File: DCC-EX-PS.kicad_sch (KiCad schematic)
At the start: 8 parts, among them J1 54-00129, J2 OSTVN03A150, U1 TSR 0.5-2450, U2 TSR 2-24120

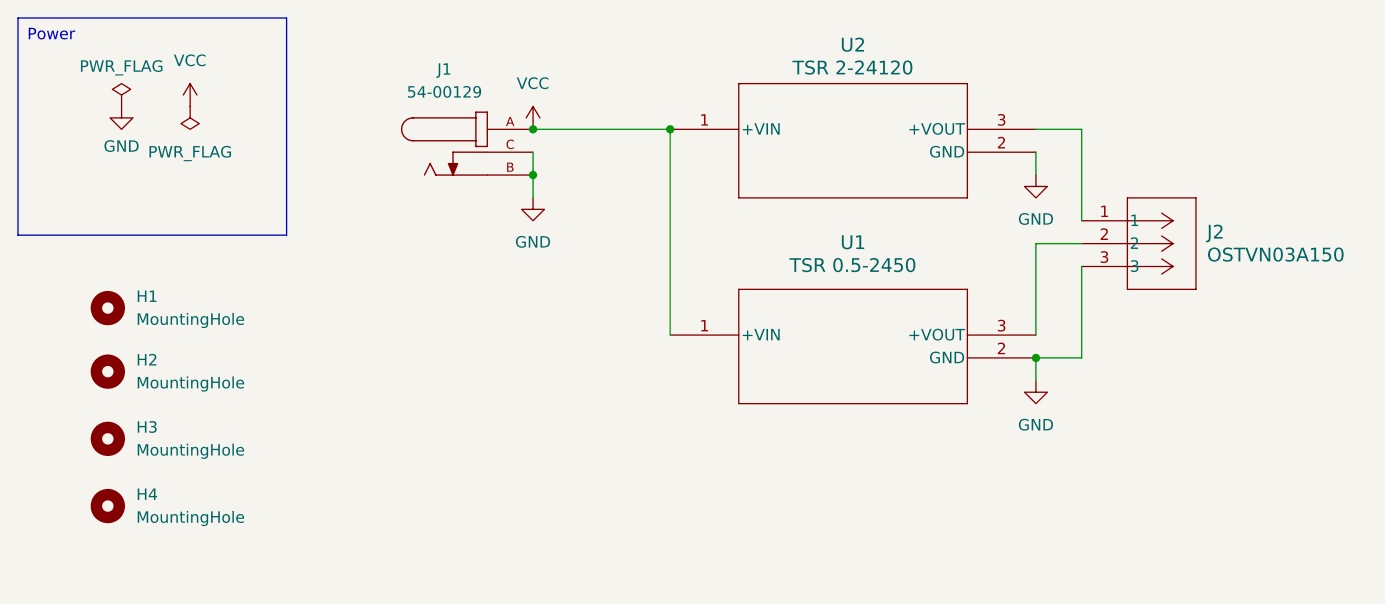
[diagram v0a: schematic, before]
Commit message: Added more graphics and 24v out terminal
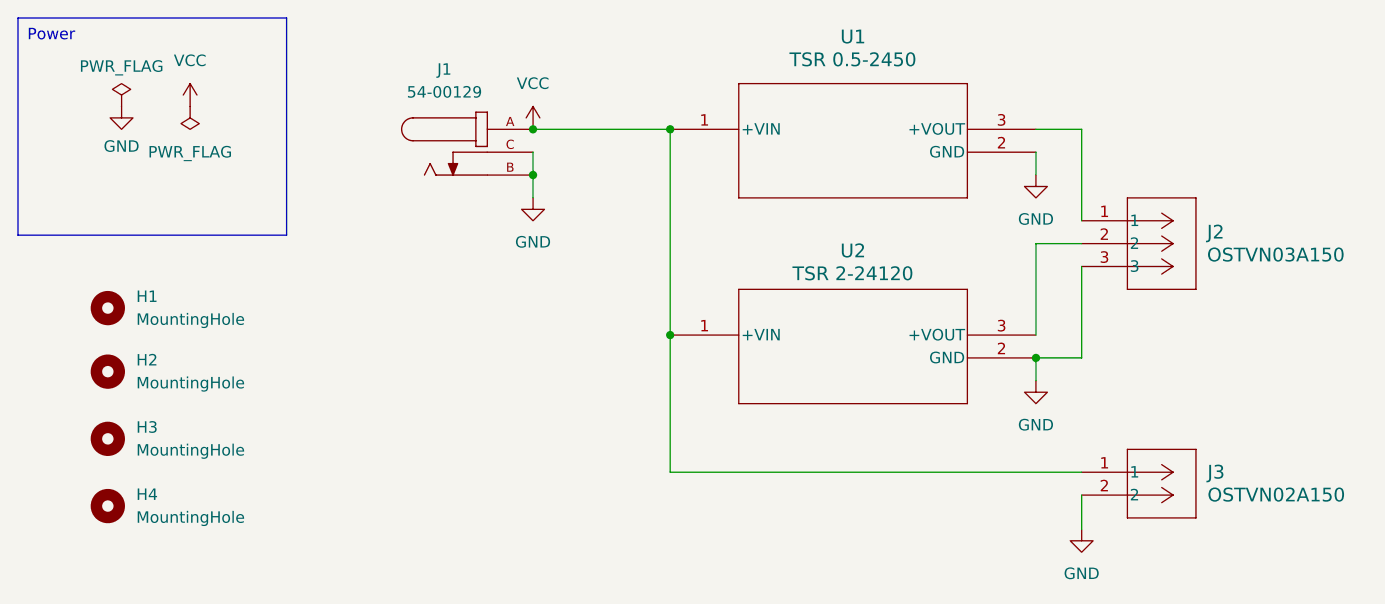
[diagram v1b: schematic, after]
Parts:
- added J3: OSTVN02A150, CONN_OSTVN02A150_OST, symbol DCC-EX-symbols:OSTVN02A150
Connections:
- net GND: now also J3.2
- net VCC: now also J3.1
- net at U1.3 (+VOUT): now also J2.1; no longer J2.2
- net at U2.3 (+VOUT): now also J2.2; no longer J2.1
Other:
- moved on the sheet: U1, U2
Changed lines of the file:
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@@
   (junction (at 106.68 50.8) (diameter 0) (color 0 0 0 0)
   )
+  (junction (at 121.92 68.58) (diameter 0) (color 0 0 0 0)
+  )
+  (junction (at 121.92 45.72) (diameter 0) (color 0 0 0 0)
+  )
   (junction (at 106.68 45.72) (diameter 0) (color 0 0 0 0)
   )
-  (junction (at 121.92 45.72) (diameter 0) (color 0 0 0 0)
-  )
   (junction (at 162.56 71.12) (diameter 0) (color 0 0 0 0)
   )
@@
     (stroke (width 0) (type default))
   )
+  (wire (pts (xy 167.64 86.36) (xy 167.64 90.17))
+    (stroke (width 0) (type default))
+  )
+  (wire (pts (xy 121.92 83.82) (xy 167.64 83.82))
+    (stroke (width 0) (type default))
+  )
   (wire (pts (xy 121.92 45.72) (xy 121.92 68.58))
+    (stroke (width 0) (type default))
+  )
+  (wire (pts (xy 121.92 68.58) (xy 121.92 83.82))
     (stroke (width 0) (type default))
   )
@@
     )
   )
-  (symbol (lib_id "DCC-EX-symbols:TSR_0.5-2450") (at 121.92 68.58 0) (unit 1)
-    (in_bom yes) (on_board yes) (dnp no) (fields_autoplaced)
-    (property "Reference" "U1" (at 142.24 58.3184 0)
+  (symbol (lib_id "DCC-EX-symbols:TSR_0.5-2450") (at 121.92 45.72 0) (unit 1)
+    (in_bom yes) (on_board yes) (dnp no) (fields_autoplaced)
+    (property "Reference" "U1" (at 142.24 35.4584 0)
       (effects (font (size 1.524 1.524)))
     )
-    (property "Value" "TSR 0.5-2450" (at 142.24 60.8584 0)
+    (property "Value" "TSR 0.5-2450" (at 142.24 37.9984 0)
       (effects (font (size 1.524 1.524)))
     )
-    (property "Footprint" "TSR0P5_TRP" (at 121.92 68.58 0)
-      (effects (font (size 1.27 1.27) italic) hide)
-    )
-    (property "Datasheet" "TSR 0.5-2450" (at 121.92 68.58 0)
+    (property "Footprint" "TSR0P5_TRP" (at 121.92 45.72 0)
+      (effects (font (size 1.27 1.27) italic) hide)
+    )
+    (property "Datasheet" "TSR 0.5-2450" (at 121.92 45.72 0)
       (effects (font (size 1.27 1.27) italic) hide)
     )
@@
     )
   )
-  (symbol (lib_id "DCC-EX-symbols:TSR_2-24120") (at 121.92 45.72 0) (unit 1)
-    (in_bom yes) (on_board yes) (dnp no) (fields_autoplaced)
-    (property "Reference" "U2" (at 142.24 36.3728 0)
+  (symbol (lib_id "power:GND") (at 167.64 90.17 0) (unit 1)
+    (in_bom yes) (on_board yes) (dnp no) (fields_autoplaced)
+    (property "Reference" "#PWR07" (at 167.64 96.52 0)
+      (effects (font (size 1.27 1.27)) hide)
+    )
+    (property "Value" "GND" (at 167.64 95.0976 0)
+      (effects (font (size 1.27 1.27)))
+    )
+    (property "Footprint" "" (at 167.64 90.17 0)
+      (effects (font (size 1.27 1.27)) hide)
+    )
+    (property "Datasheet" "" (at 167.64 90.17 0)
+      (effects (font (size 1.27 1.27)) hide)
+    )
+    (pin "1")
+    (instances
+      (project "DCC-EX-PS"
+        (path "/240d2133-ff7a-420a-95de-a58563a16dc1"
+          (reference "#PWR07") (unit 1)
+        )
+      )
+    )
+  )
+  (symbol (lib_id "DCC-EX-symbols:OSTVN02A150") (at 167.64 83.82 0) (unit 1)
+    (in_bom yes) (on_board yes) (dnp no) (fields_autoplaced)
+    (property "Reference" "J3" (at 181.61 83.82 0)
+      (effects (font (size 1.524 1.524)) (justify left))
+    )
+    (property "Value" "OSTVN02A150" (at 181.61 86.36 0)
+      (effects (font (size 1.524 1.524)) (justify left))
+    )
+    (property "Footprint" "CONN_OSTVN02A150_OST" (at 167.64 83.82 0)
+      (effects (font (size 1.27 1.27) italic) hide)
+    )
+    (property "Datasheet" "OSTVN02A150" (at 167.64 83.82 0)
+      (effects (font (size 1.27 1.27) italic) hide)
+    )
+    (pin "1")
+    (pin "2")
+    (instances
+      (project "DCC-EX-PS"
+        (path "/240d2133-ff7a-420a-95de-a58563a16dc1"
+          (reference "J3") (unit 1)
+        )
+      )
+    )
+  )
+  (symbol (lib_id "DCC-EX-symbols:TSR_2-24120") (at 121.92 68.58 0) (unit 1)
+    (in_bom yes) (on_board yes) (dnp no) (fields_autoplaced)
+    (property "Reference" "U2" (at 142.24 59.2328 0)
       (effects (font (size 1.524 1.524)))
     )
-    (property "Value" "TSR 2-24120" (at 142.24 38.9128 0)
+    (property "Value" "TSR 2-24120" (at 142.24 61.7728 0)
       (effects (font (size 1.524 1.524)))
     )
-    (property "Footprint" "TSR2-SINGLE_TRP" (at 121.92 45.72 0)
-      (effects (font (size 1.27 1.27) italic) hide)
-    )
-    (property "Datasheet" "TSR 2-24120" (at 121.92 45.72 0)
-      (effects (font (size 1.27 1.27) italic) hide)
-    )
+    (property "Footprint" "TSR2-SINGLE_TRP" (at 121.92 68.58 0)
+      (effects (font (size 1.27 1.27) italic) hide)
+    )
+    (property "Datasheet" "TSR 2-24120" (at 121.92 68.58 0)
+      (effects (font (size 1.27 1.27) italic) hide)
+    )
